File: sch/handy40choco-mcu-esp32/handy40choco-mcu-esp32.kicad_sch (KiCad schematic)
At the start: 15 parts, among them J1 Conn_01x02

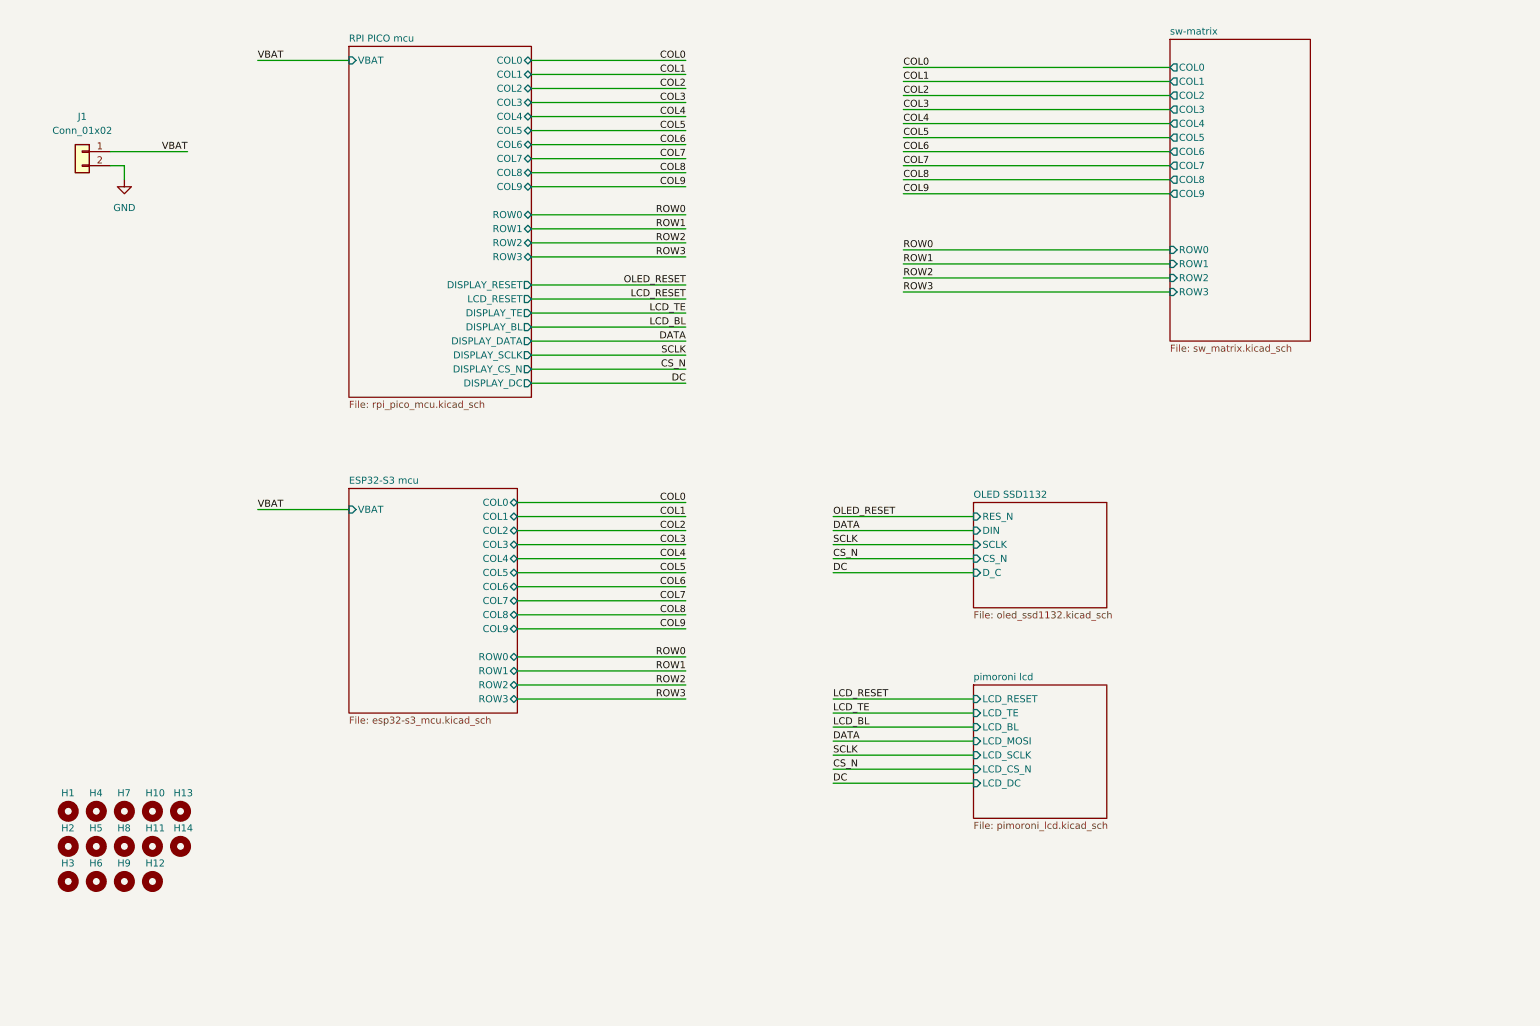
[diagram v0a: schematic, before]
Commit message: マイコン基板(ESP32-S3)の雛形です。
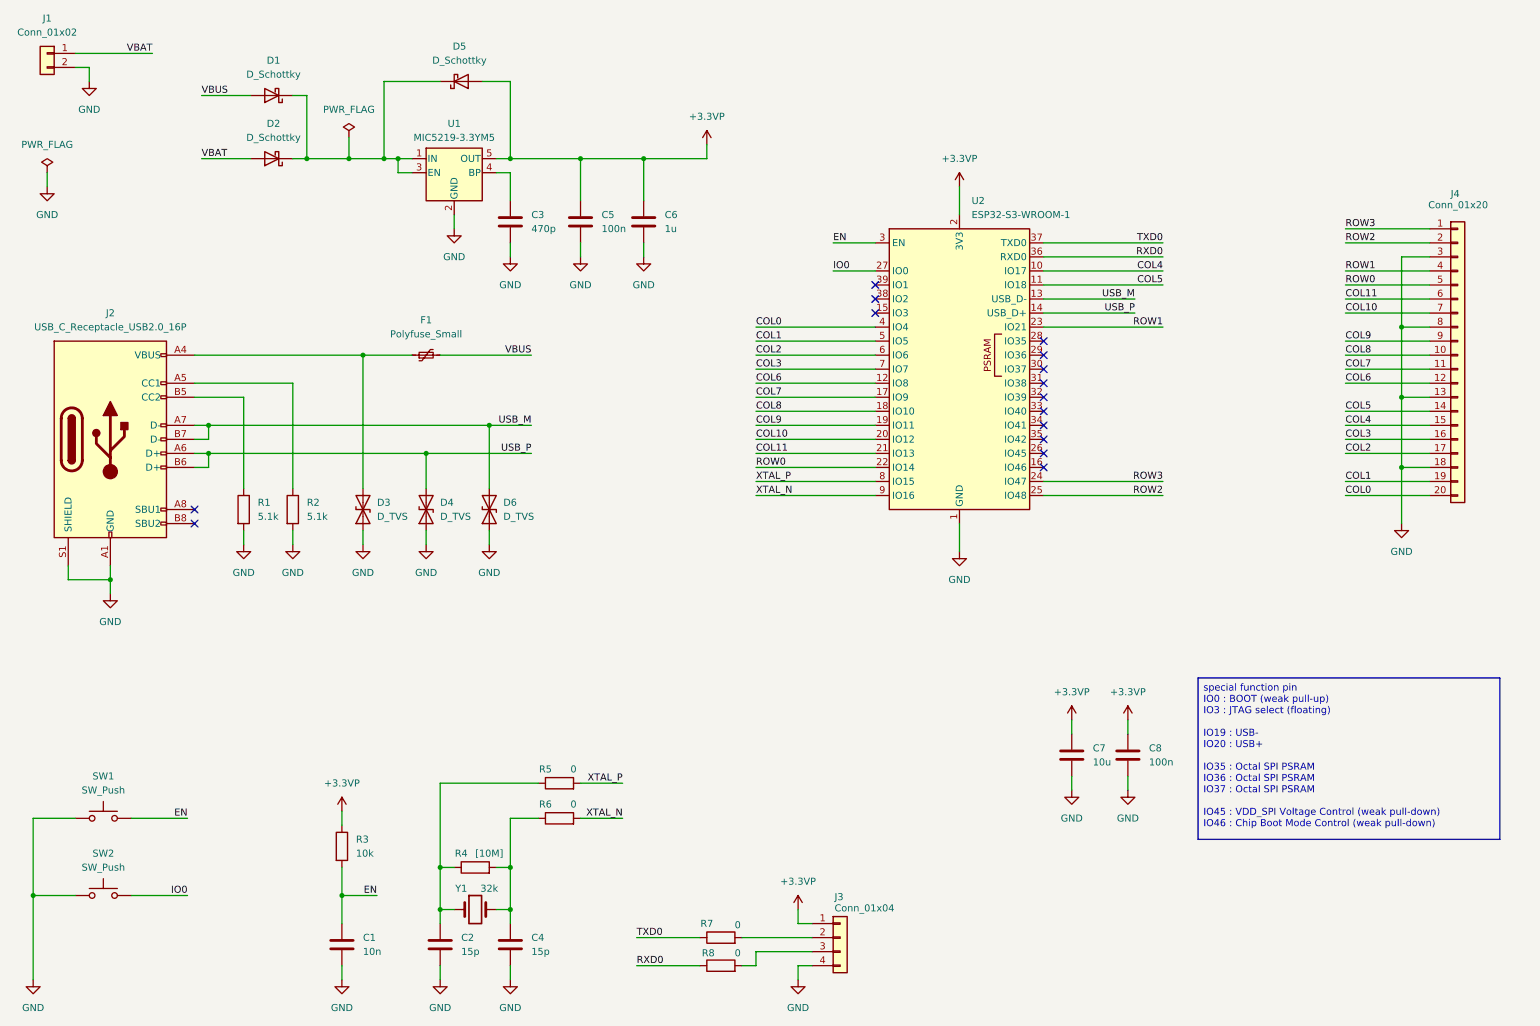
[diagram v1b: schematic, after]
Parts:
- removed H1, H10, H11, H12, H13, H14, H2, H3, H4, H5, H6, H7, H8, H9: MountingHole, my_keyswitch:my_MountingHole_2.2mm_M2, symbol Mechanical:MountingHole
- added C1: 10n, Capacitor_SMD:C_0603_1608Metric_Pad1.08x0.95mm_HandSolder, symbol Device:C
- added C2, C4: 15p, Capacitor_SMD:C_0603_1608Metric_Pad1.08x0.95mm_HandSolder, symbol Device:C
- added C3: 470p, Capacitor_SMD:C_0603_1608Metric_Pad1.08x0.95mm_HandSolder, symbol Device:C
- added C5, C8: 100n, Capacitor_SMD:C_0603_1608Metric_Pad1.08x0.95mm_HandSolder, symbol Device:C
- added C6: 1u, Capacitor_SMD:C_0603_1608Metric_Pad1.08x0.95mm_HandSolder, symbol Device:C
- added C7: 10u, Capacitor_SMD:C_0603_1608Metric_Pad1.08x0.95mm_HandSolder, symbol Device:C
- added D1, D2, D5: D_Schottky, Diode_SMD:D_SOD-123, symbol Device:D_Schottky
- added D3, D4, D6: D_TVS, Diode_SMD:D_SOD-123, symbol Device:D_TVS
- added F1: Polyfuse_Small, Fuse:Fuse_Littelfuse-NANO2-451_453, symbol Device:Polyfuse_Small
- added J2: USB_C_Receptacle_USB2.0_16P, Connector_USB:USB_C_Receptacle_XKB_U262-16XN-4BVC11, symbol Connector:USB_C_Receptacle_USB2.0_16P
- added J3: Conn_01x04, Connector_JST:JST_XH_B4B-XH-A_1x04_P2.50mm_Vertical, symbol Connector_Generic:Conn_01x04
- added J4: Conn_01x20, Connector_PinHeader_2.54mm:PinHeader_1x20_P2.54mm_Vertical, symbol Connector_Generic:Conn_01x20
- added R1, R2: 5.1k, Resistor_SMD:R_0603_1608Metric, symbol Device:R
- added R3: 10k, Resistor_SMD:R_0603_1608Metric, symbol Device:R
- added R4: [10M], Resistor_SMD:R_0603_1608Metric, symbol Device:R
- added R5, R6, R7, R8: 0, Resistor_SMD:R_0603_1608Metric, symbol Device:R
- added SW1, SW2: SW_Push, Button_Switch_SMD:SW_Push_SPST_NO_Alps_SKRK, symbol Switch:SW_Push
- added U1: MIC5219-3.3YM5, Package_TO_SOT_SMD:SOT-23-5, symbol Regulator_Linear:MIC5219-3.3YM5
- added U2: ESP32-S3-WROOM-1, RF_Module:ESP32-S3-WROOM-1, symbol RF_Module:ESP32-S3-WROOM-1
- added Y1: 32k, Crystal:Crystal_SMD_2012-2Pin_2.0x1.2mm_HandSoldering, symbol Device:Crystal
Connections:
- net COL0: now also J4.20 (Pin_20), U2.4 (IO4)
- net COL1: now also J4.19 (Pin_19), U2.5 (IO5)
- net COL2: now also J4.17 (Pin_17), U2.6 (IO6)
- net COL3: now also J4.16 (Pin_16), U2.7 (IO7)
- net COL4: now also J4.15 (Pin_15), U2.10 (IO17)
- net COL5: now also J4.14 (Pin_14), U2.11 (IO18)
- net COL6: now also J4.12 (Pin_12), U2.12 (IO8)
- net COL7: now also J4.11 (Pin_11), U2.17 (IO9)
- net COL8: now also J4.10 (Pin_10), U2.18 (IO10)
- net COL9: now also J4.9 (Pin_9), U2.19 (IO11)
- net GND: now also C1.2, C2.2, C3.2, C4.2, C5.2, C6.2, C7.2, C8.2, D3.1 (A1), D4.1 (A1), D6.1 (A1), J2.A1 (GND), J2.A12 (GND), J2.B1 (GND), J2.B12 (GND), J2.S1 (SHIELD), J3.4 (Pin_4), J4.13 (Pin_13), J4.18 (Pin_18), J4.3 (Pin_3), J4.8 (Pin_8), R1.2, R2.2, SW1.1, SW2.1, U1.2 (GND), U2.1 (GND), U2.40 (GND), U2.41 (GND)
- net ROW0: now also J4.5 (Pin_5), U2.22 (IO14)
- net ROW1: now also J4.4 (Pin_4), U2.23 (IO21)
- net ROW2: now also J4.2 (Pin_2), U2.25 (IO48)
- net ROW3: now also J4.1 (Pin_1), U2.24 (IO47)
- net VBAT: now also D2.2 (A)
- new net: J3.2 (Pin_2), R7.2
- new net: J3.3 (Pin_3), R8.2
- new net: C2.1, R4.1, R5.1, Y1.1
- new net: C4.1, R4.2, R6.1, Y1.2
- new net: D3.2 (A2), F1.1, J2.A4 (VBUS), J2.A9 (VBUS), J2.B4 (VBUS), J2.B9 (VBUS)
- new net: D1.1 (K), D2.1 (K), D5.1 (K), U1.1 (IN), U1.3 (EN)
- new net: J2.A5 (CC1), R2.1
- new net: C3.1, U1.4 (BP)
- new net: J2.B5 (CC2), R1.1
- new net +3.3VP: C5.1, C6.1, C7.1, C8.1, D5.2 (A), J3.1 (Pin_1), R3.1, U1.5 (OUT), U2.2 (3V3)
- new net COL10: J4.7 (Pin_7), U2.20 (IO12)
- new net COL11: J4.6 (Pin_6), U2.21 (IO13)
- new net EN: C1.1, R3.2, SW1.2, U2.3 (EN)
- new net IO0: SW2.2, U2.27 (IO0)
- new net RXD0: R8.1, U2.36 (RXD0)
- new net TXD0: R7.1, U2.37 (TXD0)
- new net USB_M: D6.2 (A2), J2.A7 (D-), J2.B7 (D-), U2.13 (USB_D-)
- new net USB_P: D4.2 (A2), J2.A6 (D+), J2.B6 (D+), U2.14 (USB_D+)
- new net VBUS: D1.2 (A), F1.2
- new net XTAL_N: R6.2, U2.9 (IO16)
- new net XTAL_P: R5.2, U2.8 (IO15)
- no-connect marks 0 -> 15
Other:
- removed sheet ESP32-S3 mcu
- removed sheet OLED SSD1132
- removed sheet RPI PICO mcu
- removed sheet pimoroni lcd
- removed sheet sw-matrix
- moved on the sheet: J1
